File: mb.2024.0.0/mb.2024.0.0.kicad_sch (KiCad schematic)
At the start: 22 parts, among them J1 DSP_out_12v_GND, J10 DSP+, J11 Screw_Terminal_VMN, J13 Connector_I2C_for_mux, J16 RX_bat, J17 DSP GND, J18 ELEC_M, J19 ELEC_N, J2 DPS5005_input_0_to_50V, J3 Screw_Terminal_AB, J4 Conn_01x08_Female, J5 Conn_01x04_Female, J6 Conn_01x08_Female, J7 Raspberry_Pi_2_3, J8 Connector_I2C_for_MCP23008, J9 TX_bat, U1 MCP23008-xP, U3 24LC02

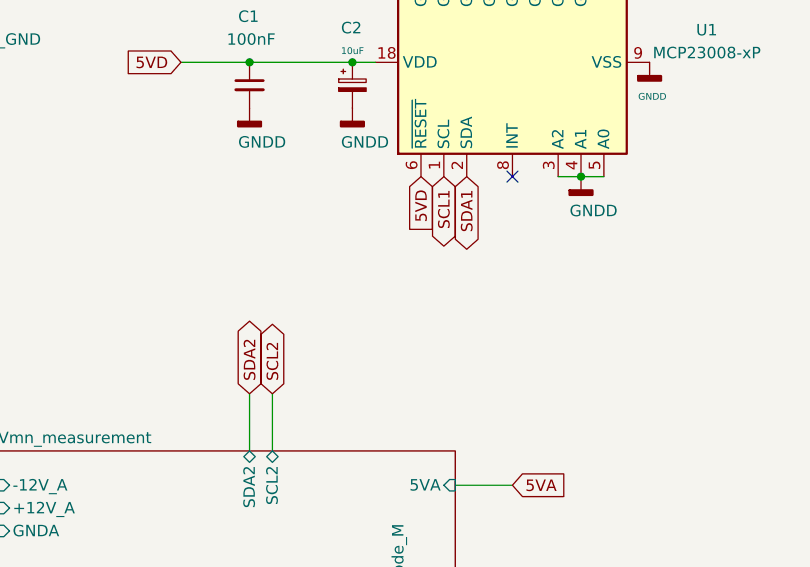
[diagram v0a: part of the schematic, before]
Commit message: update measurement board schematics and circuit
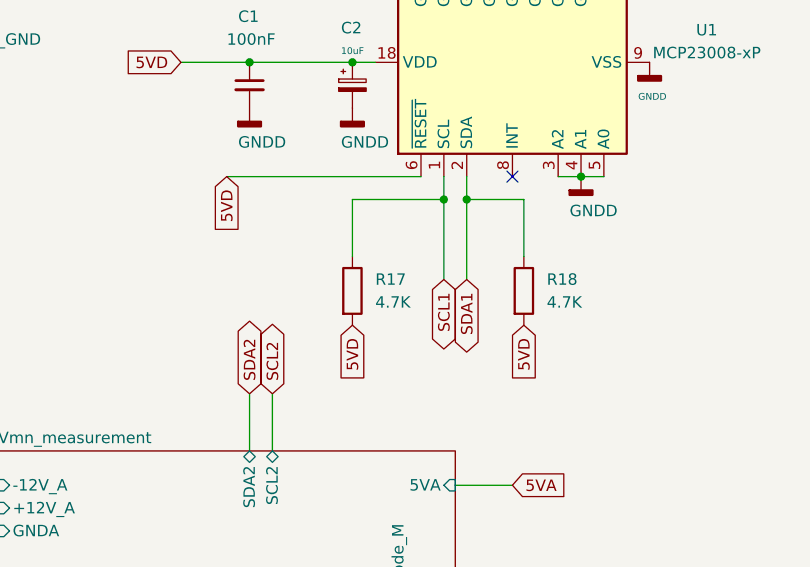
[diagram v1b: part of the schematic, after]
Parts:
- added R17, R18: 4.7K, Resistor_THT:R_Axial_DIN0207_L6.3mm_D2.5mm_P7.62mm_Horizontal, symbol Device:R
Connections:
- net 5VD: now also R17.2, R18.2
- net SCL1: now also R17.1
- net SDA1: now also R18.1
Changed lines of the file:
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@@
   (junction (at 180.34 45.72) (diameter 0) (color 0 0 0 0)
   )
+  (junction (at 149.86 106.68) (diameter 0) (color 0 0 0 0)
+  )
   (junction (at 271.78 71.12) (diameter 0) (color 0 0 0 0)
   )
@@
   )
   (junction (at 142.24 157.48) (diameter 0) (color 0 0 0 0)
+  )
+  (junction (at 147.32 106.68) (diameter 0) (color 0 0 0 0)
   )
   (no_connect (at 200.66 140.97))
@@
     (stroke (width 0) (type default) (color 0 0 0 0))
   )
+  (wire (pts (xy 147.32 106.68) (xy 147.32 104.14))
+    (stroke (width 0) (type default) (color 0 0 0 0))
+  )
   (wire (pts (xy 33.02 58.42) (xy 33.02 62.23))
     (stroke (width 0) (type default) (color 0 0 0 0))
@@
     (stroke (width 0) (type default) (color 0 0 0 0))
   )
+  (wire (pts (xy 156.21 113.03) (xy 156.21 106.68))
+    (stroke (width 0) (type default) (color 0 0 0 0))
+  )
   (wire (pts (xy 160.02 77.47) (xy 160.02 78.74))
     (stroke (width 0) (type default) (color 0 0 0 0))
@@
     (stroke (width 0) (type default) (color 0 0 0 0))
   )
+  (wire (pts (xy 137.16 106.68) (xy 147.32 106.68))
+    (stroke (width 0) (type default) (color 0 0 0 0))
+  )
   (wire (pts (xy 30.48 86.36) (xy 39.37 86.36))
     (stroke (width 0) (type default) (color 0 0 0 0))
@@
     (stroke (width 0) (type default) (color 0 0 0 0))
   )
+  (wire (pts (xy 123.19 104.14) (xy 144.78 104.14))
+    (stroke (width 0) (type default) (color 0 0 0 0))
+  )
   (wire (pts (xy 64.77 173.99) (xy 85.09 173.99))
     (stroke (width 0) (type default) (color 0 0 0 0))
@@
     (stroke (width 0) (type default) (color 0 0 0 0))
   )
+  (wire (pts (xy 147.32 115.57) (xy 147.32 106.68))
+    (stroke (width 0) (type default) (color 0 0 0 0))
+  )
   (wire (pts (xy 267.97 55.88) (xy 267.97 58.42))
     (stroke (width 0) (type default) (color 0 0 0 0))
@@
     (stroke (width 0) (type default) (color 0 0 0 0))
   )
+  (wire (pts (xy 149.86 115.57) (xy 149.86 106.68))
+    (stroke (width 0) (type default) (color 0 0 0 0))
+  )
   (wire (pts (xy 259.08 100.33) (xy 264.16 100.33))
     (stroke (width 0) (type default) (color 0 0 0 0))
@@
     (stroke (width 0) (type default) (color 0 0 0 0))
   )
+  (wire (pts (xy 137.16 113.03) (xy 137.16 106.68))
+    (stroke (width 0) (type default) (color 0 0 0 0))
+  )
   (wire (pts (xy 255.27 109.22) (xy 264.16 109.22))
     (stroke (width 0) (type default) (color 0 0 0 0))
@@
     (stroke (width 0) (type default) (color 0 0 0 0))
   )
+  (wire (pts (xy 149.86 106.68) (xy 149.86 104.14))
+    (stroke (width 0) (type default) (color 0 0 0 0))
+  )
   (wire (pts (xy 86.36 29.21) (xy 90.17 29.21))
     (stroke (width 0) (type default) (color 0 0 0 0))
@@
     (stroke (width 0) (type default) (color 0 0 0 0))
   )
+  (wire (pts (xy 156.21 106.68) (xy 149.86 106.68))
+    (stroke (width 0) (type default) (color 0 0 0 0))
+  )
   (global_label "GP7" (shape input) (at 259.08 97.79 180) (fields_autoplaced)
     (effects (font (size 1.27 1.27)) (justify right))
@@
     )
   )
+  (global_label "5VD" (shape input) (at 156.21 120.65 270) (fields_autoplaced)
+    (effects (font (size 1.27 1.27)) (justify right))
+    (property "Intersheet References" "${INTERSHEET_REFS}" (id 0) (at 156.1306 126.6312 90)
+      (effects (font (size 1.27 1.27)) (justify right) hide)
+    )
+  )
   (global_label "GP4" (shape input) (at 259.08 105.41 180) (fields_autoplaced)
     (effects (font (size 1.27 1.27)) (justify right))
@@
     )
   )
-  (global_label "SDA1" (shape bidirectional) (at 149.86 104.14 270) (fields_autoplaced)
-    (effects (font (size 1.27 1.27)) (justify right))
-    (property "Intersheet References" "${INTERSHEET_REFS}" (id 0) (at 149.7806 111.3307 90)
+  (global_label "SDA1" (shape bidirectional) (at 149.86 115.57 270) (fields_autoplaced)
+    (effects (font (size 1.27 1.27)) (justify right))
+    (property "Intersheet References" "${INTERSHEET_REFS}" (id 0) (at 149.7806 122.7607 90)
       (effects (font (size 1.27 1.27)) (justify right) hide)
     )
@@
     )
   )
+  (global_label "5VD" (shape input) (at 137.16 120.65 270) (fields_autoplaced)
+    (effects (font (size 1.27 1.27)) (justify right))
+    (property "Intersheet References" "${INTERSHEET_REFS}" (id 0) (at 137.0806 126.6312 90)
+      (effects (font (size 1.27 1.27)) (justify right) hide)
+    )
+  )
   (global_label "GP1" (shape input) (at 64.77 160.02 0) (fields_autoplaced)
     (effects (font (size 1.27 1.27)) (justify left))
@@
     )
   )
-  (global_label "5VD" (shape input) (at 144.78 104.14 270) (fields_autoplaced)
-    (effects (font (size 1.27 1.27)) (justify right))
-    (property "Intersheet References" "${INTERSHEET_REFS}" (id 0) (at 144.7006 110.1212 90)
+  (global_label "5VD" (shape input) (at 123.19 104.14 270) (fields_autoplaced)
+    (effects (font (size 1.27 1.27)) (justify right))
+    (property "Intersheet References" "${INTERSHEET_REFS}" (id 0) (at 123.1106 110.1212 90)
       (effects (font (size 1.27 1.27)) (justify right) hide)
     )
@@
     )
   )
-  (global_label "SCL1" (shape bidirectional) (at 147.32 104.14 270) (fields_autoplaced)
-    (effects (font (size 1.27 1.27)) (justify right))
-    (property "Intersheet References" "${INTERSHEET_REFS}" (id 0) (at 147.2406 111.2702 90)
+  (global_label "SCL1" (shape bidirectional) (at 147.32 115.57 270) (fields_autoplaced)
+    (effects (font (size 1.27 1.27)) (justify right))
+    (property "Intersheet References" "${INTERSHEET_REFS}" (id 0) (at 147.2406 122.7002 90)
       (effects (font (size 1.27 1.27)) (justify right) hide)
     )
@@
     )
     (pin "1")
+  )
+  (symbol (lib_id "Device:R") (at 137.16 116.84 0) (unit 1)
+    (in_bom yes) (on_board yes) (fields_autoplaced)
+    (property "Reference" "R17" (id 0) (at 139.7 115.5699 0)
+      (effects (font (size 1.27 1.27)) (justify left))
+    )
+    (property "Value" "4.7K" (id 1) (at 139.7 118.1099 0)
+      (effects (font (size 1.27 1.27)) (justify left))
+    )
+    (property "Footprint" "Resistor_THT:R_Axial_DIN0207_L6.3mm_D2.5mm_P7.62mm_Horizontal" (id 2) (at 135.382 116.84 90)
+      (effects (font (size 1.27 1.27)) hide)
+    )
+    (property "Datasheet" "~" (id 3) (at 137.16 116.84 0)
+      (effects (font (size 1.27 1.27)) hide)
+    )
+    (pin "1")
+    (pin "2")
   )
   (symbol (lib_id "power:GNDD") (at 231.14 91.44 0) (unit 1)
@@
     (pin "6")
   )
+  (symbol (lib_id "Device:R") (at 156.21 116.84 0) (unit 1)
+    (in_bom yes) (on_board yes) (fields_autoplaced)
+    (property "Reference" "R18" (id 0) (at 158.75 115.5699 0)
+      (effects (font (size 1.27 1.27)) (justify left))
+    )
+    (property "Value" "4.7K" (id 1) (at 158.75 118.1099 0)
+      (effects (font (size 1.27 1.27)) (justify left))
+    )
+    (property "Footprint" "Resistor_THT:R_Axial_DIN0207_L6.3mm_D2.5mm_P7.62mm_Horizontal" (id 2) (at 154.432 116.84 90)
+      (effects (font (size 1.27 1.27)) hide)
+    )
+    (property "Datasheet" "~" (id 3) (at 156.21 116.84 0)
+      (effects (font (size 1.27 1.27)) hide)
+    )
+    (pin "1")
+    (pin "2")
+  )
   (sheet (at 21.59 153.67) (size 43.18 24.13) (fields_autoplaced)
     (stroke (width 0.1524) (type solid) (color 0 0 0 0))
@@
       (reference "D6") (unit 1) (value "BAT86") (footprint "Diode_THT:D_DO-35_SOD27_P7.62mm_Horizontal")
     )
-    (path "/b2026999-6d31-4d17-9f3d-996babd42897/315e3262-5f7c-49e4-92d5-7463f07b52e2"
-      (reference "D7") (unit 1) (value "BAT86") (footprint "Diode_THT:D_DO-35_SOD27_P7.62mm_Horizontal")
-    )
-    (path "/b2026999-6d31-4d17-9f3d-996babd42897/01267143-7ffa-4af9-8ce8-f6a5818034cd"
-      (reference "D8") (unit 1) (value "BAT86") (footprint "Diode_THT:D_DO-35_SOD27_P7.62mm_Horizontal")
-    )
     (path "/3a1d549c-401c-4ddf-9a51-4b7588f9097f/0e7e4a4e-3291-4cc6-9e41-b290afaf5456"
       (reference "D9") (unit 1) (value "1N4001") (footprint "Diode_THT:D_DO-41_SOD81_P10.16mm_Horizontal")
@@
       (reference "R16") (unit 1) (value "100k") (footprint "Resistor_THT:R_Axial_DIN0207_L6.3mm_D2.5mm_P7.62mm_Horizontal")
     )
+    (path "/1fc08b13-9eb3-4634-8236-1f92457baff3"
+      (reference "R17") (unit 1) (value "4.7K") (footprint "Resistor_THT:R_Axial_DIN0207_L6.3mm_D2.5mm_P7.62mm_Horizontal")
+    )
+    (path "/fe83df3c-22ea-442b-82b5-e99a099a3893"
+      (reference "R18") (unit 1) (value "4.7K") (footprint "Resistor_THT:R_Axial_DIN0207_L6.3mm_D2.5mm_P7.62mm_Horizontal")
+    )
     (path "/b2026999-6d31-4d17-9f3d-996babd42897/eddcd997-356c-4d0a-b454-1e807ee28ce4"

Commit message: update pcb
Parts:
- added J? (x2): Conn_01x04_Female, symbol Connector:Conn_01x04_Female
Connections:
- net SCL1: now also J?.1 (Pin_1)
- net SDA1: now also J?.2 (Pin_2)
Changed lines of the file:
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@@
+    (stroke (width 0) (type default) (color 0 0 0 0))
+  )
+  (wire (pts (xy 247.65 20.32) (xy 251.46 20.32))
     (stroke (width 0) (type default) (color 0 0 0 0))
   )
@@
     (stroke (width 0) (type default) (color 0 0 0 0))
   )
+  (wire (pts (xy 247.65 17.78) (xy 251.46 17.78))
+    (stroke (width 0) (type default) (color 0 0 0 0))
+  )
   (wire (pts (xy 142.24 157.48) (xy 138.43 157.48))
     (stroke (width 0) (type default) (color 0 0 0 0))
@@
     )
   )
+  (global_label "SCL1" (shape bidirectional) (at 247.65 17.78 180) (fields_autoplaced)
+    (effects (font (size 1.27 1.27)) (justify right))
+    (property "Intersheet References" "${INTERSHEET_REFS}" (id 0) (at 240.5198 17.7006 0)
+      (effects (font (size 1.27 1.27)) (justify right) hide)
+    )
+  )
   (global_label "GP0" (shape input) (at 64.77 157.48 0) (fields_autoplaced)
     (effects (font (size 1.27 1.27)) (justify left))
@@
     (effects (font (size 1.27 1.27)) (justify right))
     (property "Intersheet References" "${INTERSHEET_REFS}" (id 0) (at 71.4283 24.0506 0)
+      (effects (font (size 1.27 1.27)) (justify right) hide)
+    )
+  )
+  (global_label "SDA1" (shape bidirectional) (at 247.65 20.32 180) (fields_autoplaced)
+    (effects (font (size 1.27 1.27)) (justify right))
+    (property "Intersheet References" "${INTERSHEET_REFS}" (id 0) (at 240.4593 20.2406 0)
       (effects (font (size 1.27 1.27)) (justify right) hide)
     )
@@
     )
     (pin "1")
+  )
+  (symbol (lib_id "Connector:Conn_01x04_Female") (at 267.97 20.32 0) (mirror y) (unit 1)
+    (in_bom yes) (on_board yes)
+    (property "Reference" "J?" (id 0) (at 268.605 12.7 0))
+    (property "Value" "Conn_01x04_Female" (id 1) (at 271.78 13.97 0))
+    (property "Footprint" "" (id 2) (at 267.97 20.32 0)
+      (effects (font (size 1.27 1.27)) hide)
+    )
+    (property "Datasheet" "~" (id 3) (at 267.97 20.32 0)
+      (effects (font (size 1.27 1.27)) hide)
+    )
+    (pin "1")
+    (pin "2")
+    (pin "3")
+    (pin "4")
   )
   (symbol (lib_id "Device:R") (at 137.16 116.84 0) (unit 1)
@@
     (pin "9")
   )
+  (symbol (lib_id "Connector:Conn_01x04_Female") (at 256.54 20.32 0) (unit 1)
+    (in_bom yes) (on_board yes)
+    (property "Reference" "J?" (id 0) (at 257.81 20.3199 0)
+      (effects (font (size 1.27 1.27)) (justify left))
+    )
+    (property "Value" "Conn_01x04_Female" (id 1) (at 246.38 27.94 0)
+      (effects (font (size 1.27 1.27)) (justify left))
+    )
+    (property "Footprint" "" (id 2) (at 256.54 20.32 0)
+      (effects (font (size 1.27 1.27)) hide)
+    )
+    (property "Datasheet" "~" (id 3) (at 256.54 20.32 0)
+      (effects (font (size 1.27 1.27)) hide)
+    )
+    (pin "1")
+    (pin "2")
+    (pin "3")
+    (pin "4")
+  )
   (symbol (lib_id "power:GNDD") (at 255.27 81.28 0) (unit 1)
     (in_bom yes) (on_board yes) (fields_autoplaced)
@@
       (reference "J21") (unit 1) (value "shunt -") (footprint "Connector_PinHeader_2.54mm:PinHeader_1x01_P2.54mm_Vertical")
     )
+    (path "/15a23eee-5975-4755-b1b0-cd09ad193c00"
+      (reference "J?") (unit 1) (value "Conn_01x04_Female") (footprint "")
+    )
+    (path "/99ab4477-5bb9-4eb2-ada0-903b9f73815a"
+      (reference "J?") (unit 1) (value "Conn_01x04_Female") (footprint "")
+    )
     (path "/433fb79c-38b7-4d80-8278-5eb2a5e83393/3be27309-3160-4185-86f9-1c67d16e946d"
